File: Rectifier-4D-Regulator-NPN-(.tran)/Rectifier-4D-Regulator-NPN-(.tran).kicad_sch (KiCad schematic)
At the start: 14 parts, among them Q1 BDX53C, U1 LM317_TO-220

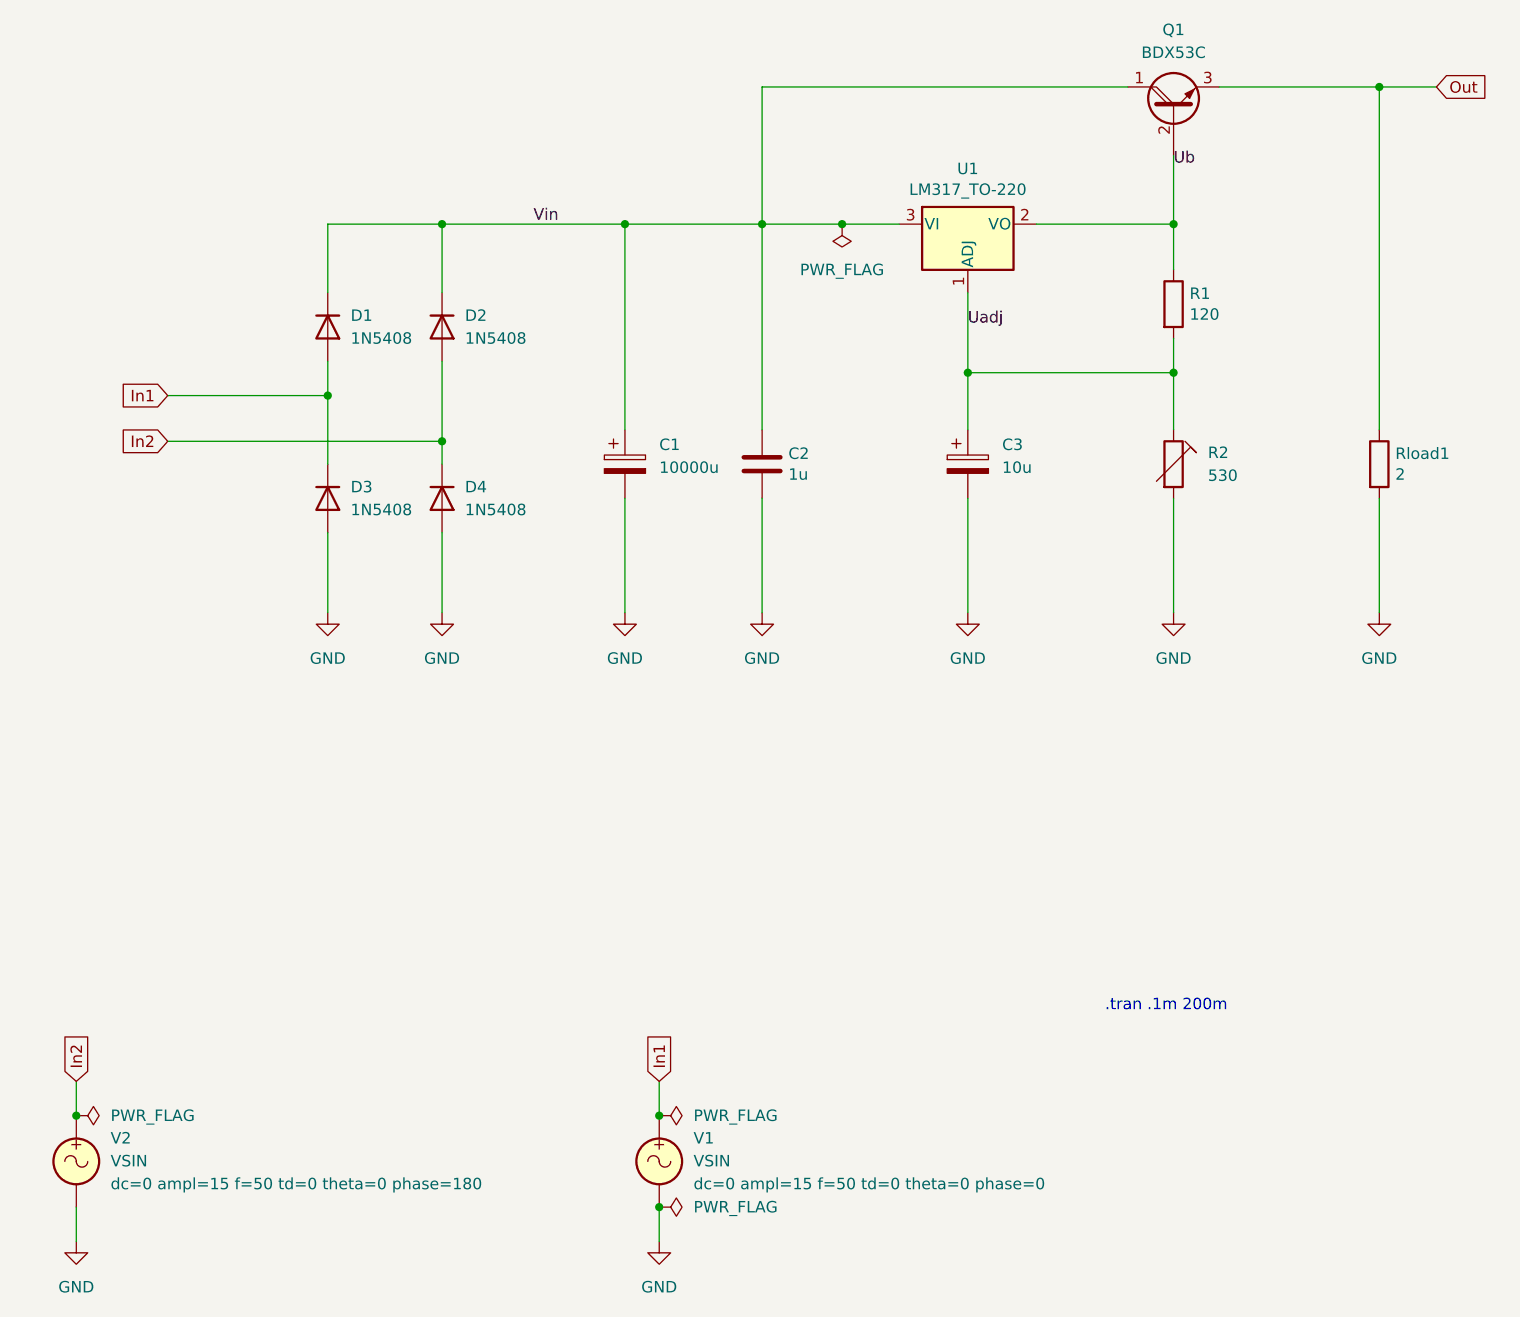
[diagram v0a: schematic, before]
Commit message: Updated all schematics and prepared for KiCad 8.0
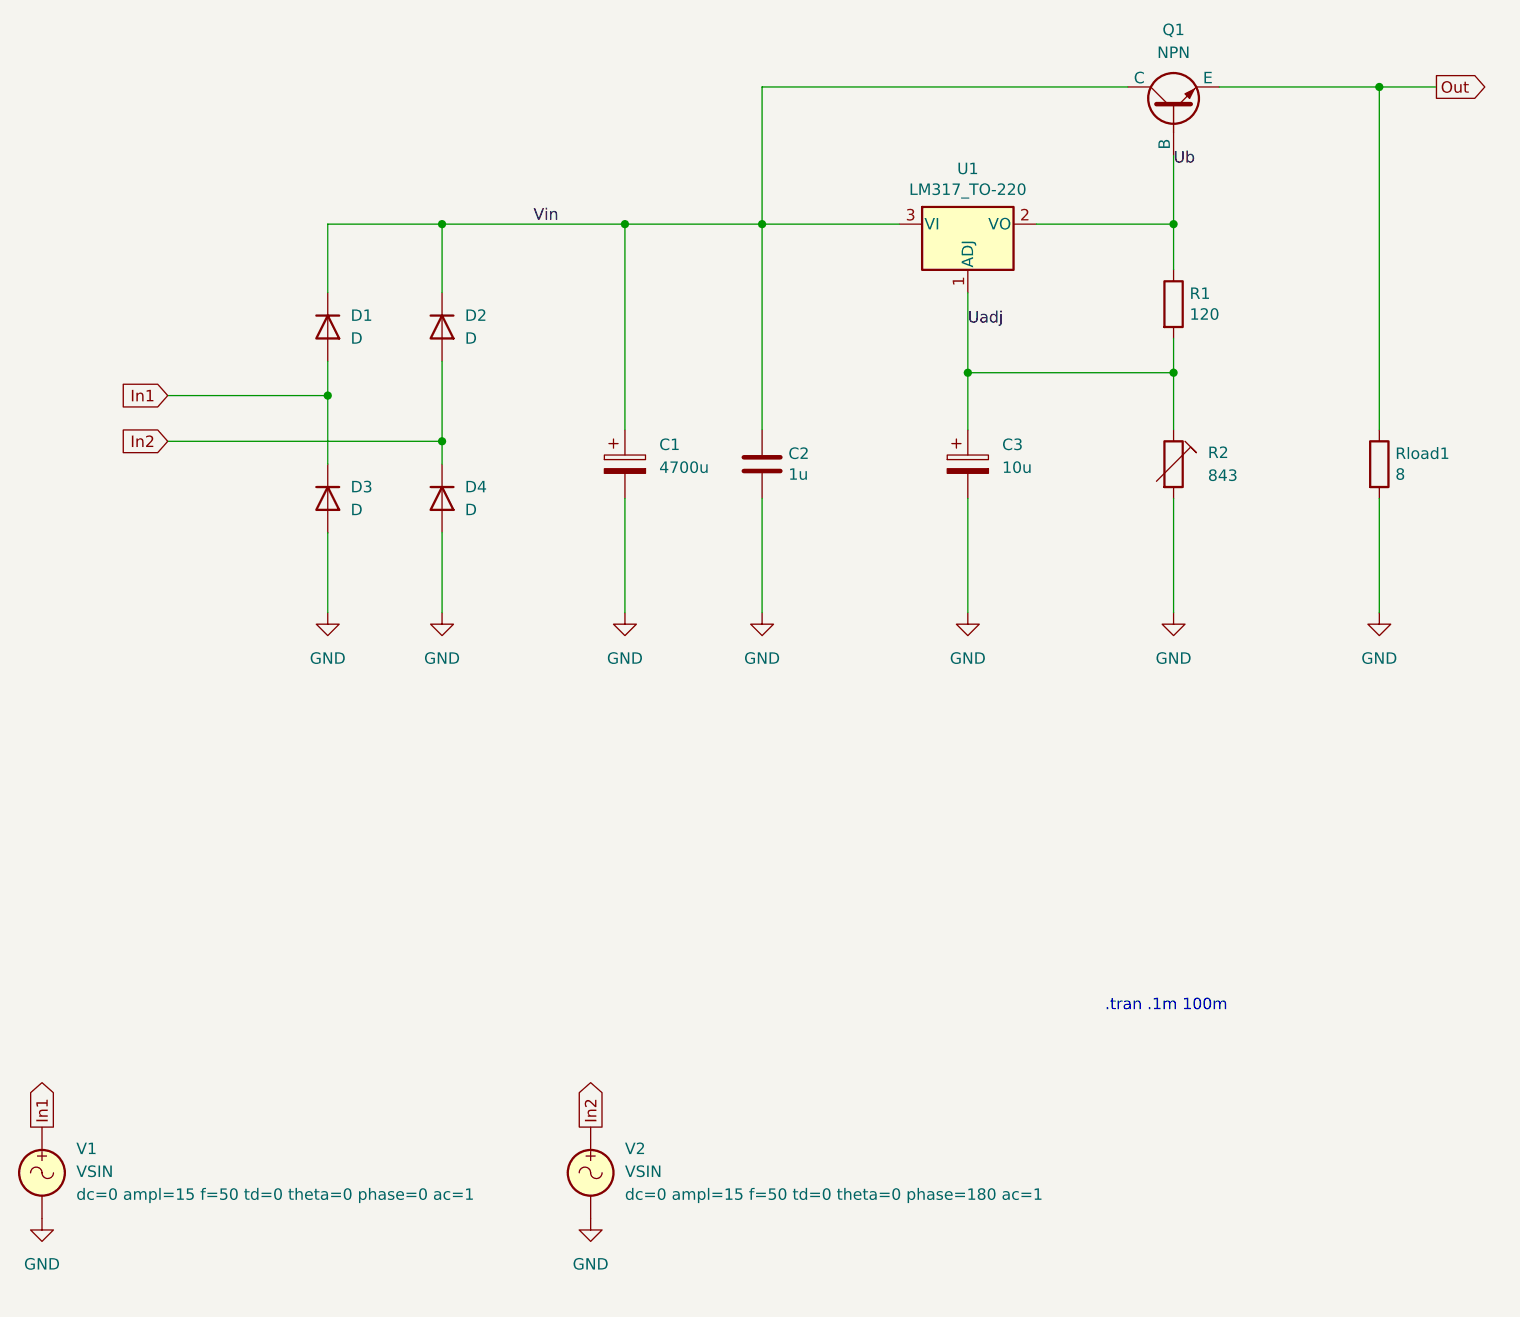
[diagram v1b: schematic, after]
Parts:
- removed Q1: BDX53C, symbol Device:Q_NPN_Darlington_CBE
- added Q1: NPN, symbol Simulation_SPICE:NPN
- C1: value 10000u -> 4700u
- D1, D2, D3, D4: value 1N5408 -> D
- R2: value 530 -> 843
- Rload1: value 2 -> 8
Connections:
- net Out: now also Q1.3 (E)
- net Ub: now also Q1.2 (B)
- net Vin: now also Q1.1 (C)
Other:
- note added: ".tran .1m 100m"
- note removed: ".tran .1m 200m"
